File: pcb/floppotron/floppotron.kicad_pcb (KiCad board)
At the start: 2 copper layers, 100 x 92 mm, 69 parts, among them J1 DIN-5_180degree, J10 Conn_01x02, J11 Conn_01x02, J2 Conn_01x02, J3 Conn_01x02, J4 Conn_01x02, J5 Conn_01x02, J6 Conn_01x02, J7 Conn_01x02, J8 AudioJack2, J9 USB_B, Q1 BC817, Q10 2N5457, Q11 BC817, Q12 BC817, Q14 BC817, Q15 BC817, Q16 BC817, Q17 BC817, Q18 BC817, Q19 BC817, Q2 BC817, Q20 BC817, Q3 BC817, Q4 BC817, Q5 BC817, Q6 BC817, Q7 BC817, Q8 BC817, Q9 BC817, U1 H11L1, U2 Pico

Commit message: redesign pcb for pico W
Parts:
- removed C1, C2: C, Capacitor_SMD:C_1206_3216Metric_Pad1.33x1.80mm_HandSolder
- removed J10, J11: Conn_01x02, Connector_JST:JST_XH_B2B-XH-A_1x02_P2.50mm_Vertical
- removed J8: AudioJack2, Connector_Audio:Jack_6.35mm_Neutrik_NRJ4HF_Horizontal
- removed JP1, JP2: Jumper, Connector_PinHeader_2.54mm:PinHeader_1x02_P2.54mm_Vertical
- removed Q10: 2N5457, Package_TO_SOT_THT:TO-92
- removed R21, R22, R23, R24: R, Resistor_SMD:R_1206_3216Metric_Pad1.30x1.75mm_HandSolder
- added H1: MountingHole_Pad, MountingHole:MountingHole_3.2mm_M3_DIN965_Pad, F.Cu at (54.0, 104.0)
- added H2: MountingHole_Pad, MountingHole:MountingHole_3.2mm_M3_DIN965_Pad, F.Cu at (146.0, 104.0)
- added H3: MountingHole_Pad, MountingHole:MountingHole_3.2mm_M3_DIN965_Pad, F.Cu at (54.0, 188.0)
- added H4: MountingHole_Pad, MountingHole:MountingHole_3.2mm_M3_DIN965_Pad, F.Cu at (146.0, 188.0)
- R1, R2: footprint Resistor_THT:R_Axial_DIN0204_L3.6mm_D1.6mm_P5.08mm_Horizontal -> Resistor_SMD:R_1206_3216Metric_Pad1.30x1.75mm_HandSolder
- U2: footprint pico:RPi_Pico_SMD_TH -> kicad-parts:RPi_Pico_debug_hole_USB_SMD_TH
- moved D1 226.3 mm to (124.7, 128.7), turned to 90 degrees
- moved R1 222.1 mm to (122.4, 125.5), turned to -90 degrees
- moved U1 212.1 mm to (118.4, 127.3), turned to 180 degrees
- moved R2 193.2 mm to (108.0, 124.9), turned to 90 degrees
- moved JP3 191.9 mm to (103.6, 124.5), turned to 180 degrees
- moved J9 178.6 mm to (131.7, 112.1)
- moved J1 178.5 mm to (113.0, 109.7)
- moved FLOPPY1 176.4 mm to (73.9, 179.2)
- moved FLOPPY2 176.4 mm to (84.1, 179.2)
- moved FLOPPY3 176.4 mm to (94.2, 179.2)
- moved FLOPPY4 176.4 mm to (104.4, 179.2)
- moved FLOPPY5 176.4 mm to (114.6, 179.2)
- moved J2 176.4 mm to (104.4, 188.1)
- moved J3 176.4 mm to (73.9, 188.1)
- moved J4 176.4 mm to (94.2, 188.1)
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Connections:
- net Net-(J9-Pad2) renamed D-
- net Net-(J9-Pad3) renamed D+
- net Net-(U1-Pad4) renamed MIDI IN
- net Net-(U1-Pad6) renamed +3V3
- J1 pad 1: Net-(J1-Pad1) -> /VCC_device
- J1 pad 2: Net-(J1-Pad2) -> GND
- J9 pad 1: Net-(J9-Pad1) -> unconnected-(J9-VBUS-Pad1)
- J9 pad 5: unconnected-(J9-Pad5) -> GND
- JP3 pad 1: Net-(J1-Pad1) -> VCC
- JP3 pad 2: VCC -> /VCC_device
- R10 pad 2: Net-(U2-Pad19) -> F0-DIR
- R11 pad 1: Net-(U2-Pad20) -> F0-STEP
- R12 pad 2: Net-(U2-Pad34) -> F5-EN
- R13 pad 2: Net-(U2-Pad32) -> F5-DIR
- R14 pad 1: Net-(U2-Pad31) -> F5-STEP
- R15 pad 2: Net-(U2-Pad29) -> F3-EN
- R16 pad 2: Net-(U2-Pad27) -> F3-DIR
- R17 pad 1: Net-(U2-Pad26) -> F3-STEP
- R18 pad 2: Net-(U2-Pad24) -> F1-EN
- R19 pad 2: Net-(U2-Pad22) -> F1-DIR
- R20 pad 1: Net-(U2-Pad21) -> F1-STEP
- R3 pad 2: Net-(U2-Pad7) -> F4-EN
- R4 pad 2: Net-(U2-Pad9) -> F4-DIR
- R5 pad 1: Net-(U2-Pad10) -> F4-STEP
- R6 pad 1: Net-(U2-Pad15) -> F2-STEP
- R7 pad 2: Net-(U2-Pad14) -> F2-DIR
- R8 pad 2: Net-(U2-Pad12) -> F2-EN
- R9 pad 2: Net-(U2-Pad17) -> F0-EN
- U2 pad 10: Net-(U2-Pad10) -> F5-EN
- U2 pad 11: unconnected-(U2-Pad11) -> F4-STEP
- U2 pad 12: Net-(U2-Pad12) -> F4-DIR
- U2 pad 13: unconnected-(U2-Pad13) -> GND
- U2 pad 14: Net-(U2-Pad14) -> F3-STEP
- U2 pad 15: Net-(U2-Pad15) -> F3-DIR
- U2 pad 16: unconnected-(U2-Pad16) -> F2-STEP
- U2 pad 17: Net-(U2-Pad17) -> F2-DIR
- U2 pad 18: unconnected-(U2-Pad18) -> GND
- U2 pad 19: Net-(U2-Pad19) -> F1-STEP
- U2 pad 20: Net-(U2-Pad20) -> F1-DIR
- U2 pad 21: Net-(U2-Pad21) -> F0-EN
- U2 pad 22: Net-(U2-Pad22) -> F0-DIR
- U2 pad 23: unconnected-(U2-Pad23) -> GND
- U2 pad 24: Net-(U2-Pad24) -> F0-STEP
- U2 pad 25: unconnected-(U2-Pad25) -> F1-EN
- U2 pad 26: Net-(U2-Pad26) -> F2-EN
- U2 pad 27: Net-(U2-Pad27) -> F3-EN
- U2 pad 28: unconnected-(U2-Pad28) -> GND
- U2 pad 29: Net-(U2-Pad29) -> F4-EN
- U2 pad 31: Net-(U2-Pad31) -> unconnected-(U2-GPIO26_ADC0-Pad31)
- U2 pad 32: Net-(U2-Pad32) -> unconnected-(U2-GPIO27_ADC1-Pad32)
- U2 pad 33: unconnected-(U2-Pad33) -> GND
- U2 pad 34: Net-(U2-Pad34) -> unconnected-(U2-GPIO28_ADC2-Pad34)
- U2 pad 7: Net-(U2-Pad7) -> F5-STEP
- U2 pad 8: unconnected-(U2-Pad8) -> GND
- U2 pad 9: Net-(U2-Pad9) -> F5-DIR
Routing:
- net GND: track 282.3 -> 0.00 mm
- net VCC: track 246.3 -> 145.4 mm, vias 1 -> 0
- net F5-EN: track 0.00 -> 69.0 mm
- net F5-DIR: track 0.00 -> 66.3 mm, vias 0 -> 1
- net F5-STEP: track 0.00 -> 62.9 mm, vias 0 -> 1
- net Net-(U2-Pad17): track 60.4 -> 0.00 mm
- net F4-DIR: track 0.00 -> 56.5 mm
- net F4-STEP: track 0.00 -> 55.6 mm, vias 0 -> 1
- net F3-DIR: track 0.00 -> 52.1 mm
- net Net-(U2-Pad19): track 48.5 -> 0.00 mm
- net F3-STEP: track 0.00 -> 47.1 mm, vias 0 -> 1
- net Net-(U2-Pad14): track 46.3 -> 0.00 mm
- net F2-DIR: track 0.00 -> 45.6 mm
- net F4-EN: track 0.00 -> 44.9 mm
- net Net-(U2-Pad9): track 44.7 -> 0.00 mm
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- added copper zone on B.Cu, net GND
- added copper zone on F.Cu, net GND
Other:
- outline, holes or cut-outs redrawn
- board text added: "Floppotron Jr. v0.4 designed by AberDerBart"
- board text removed: "D+"
- board text removed: "D-"
- board text removed: "Floppotron Jr. v0.3 designed by AberDerBart"

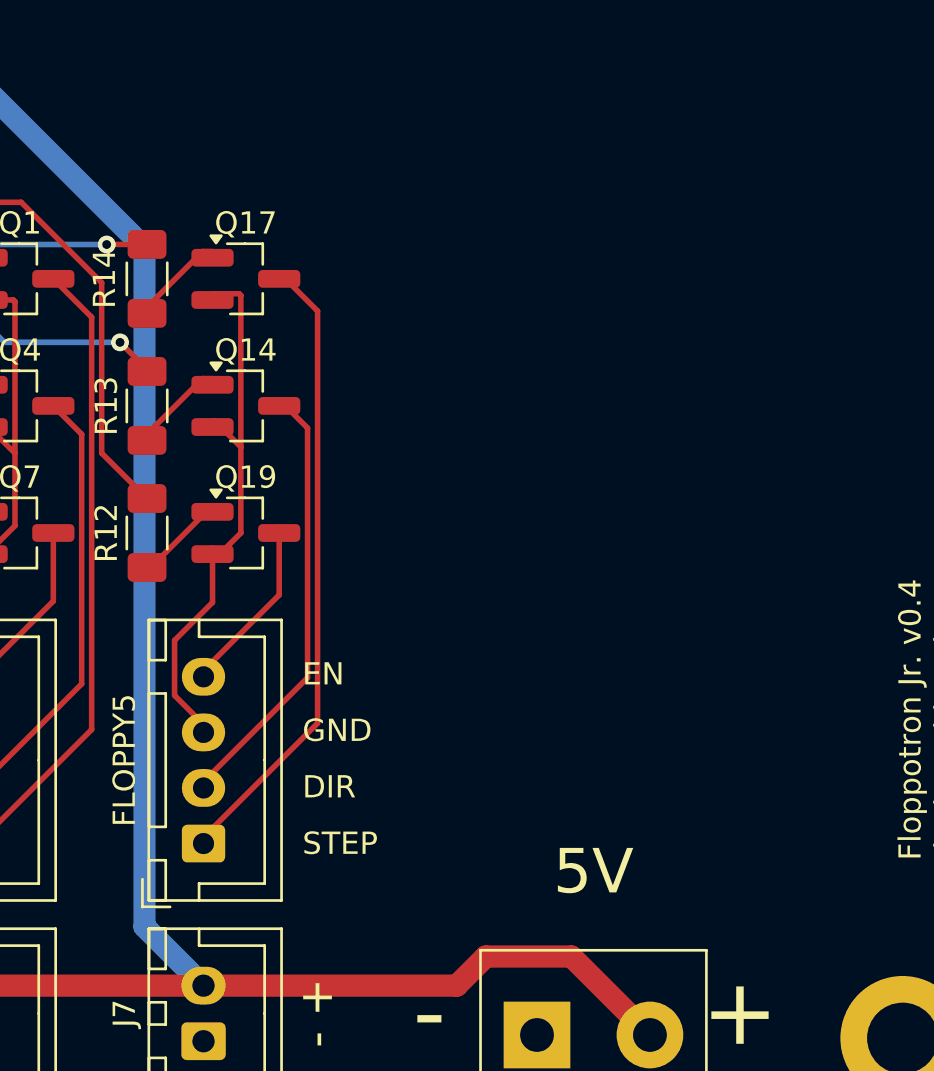
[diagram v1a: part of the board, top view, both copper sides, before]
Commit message: pcb: add kosmo power connector
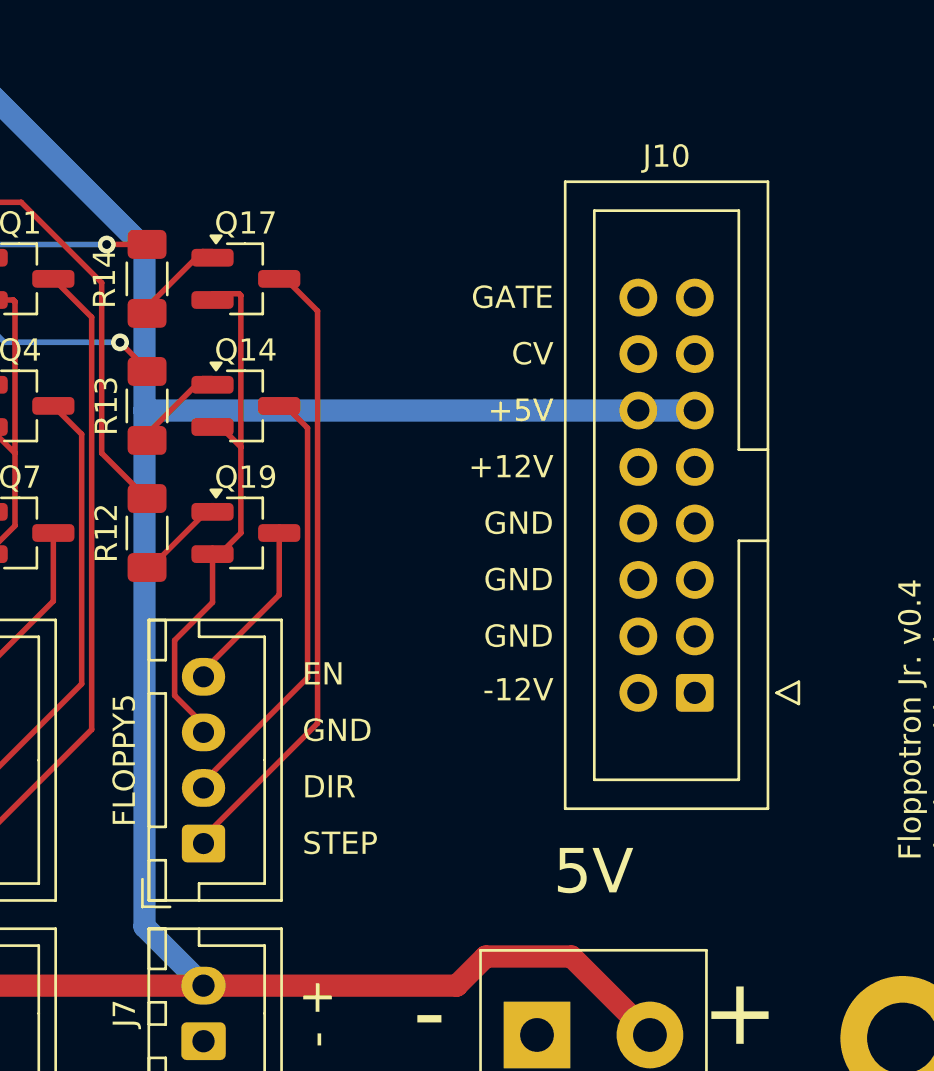
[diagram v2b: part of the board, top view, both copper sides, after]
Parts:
- added J10: Power, kosmo:Power 16 Pin, F.Cu at (135.4, 163.6)
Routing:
- net VCC: track 145.4 -> 170.2 mm
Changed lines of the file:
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@@
   (net 83 "unconnected-(U2-GPIO27_ADC1-Pad32)")
   (net 84 "unconnected-(U2-GPIO26_ADC0-Pad31)")
+  (net 85 "unconnected-(J10--12V-Pad1)")
+  (net 86 "unconnected-(J10-+12V-Pad3)")
+  (net 87 "unconnected-(J10-CV-Pad5)")
+  (net 88 "unconnected-(J10-GATE-Pad6)")
   (footprint "Connector_USB:USB_B_OST_USB-B1HSxx_Horizontal" locked (layer "F.Cu")
     (at 131.7 112.12 90)
@@
       (net 6 "GND") (pinfunction "1") (pintype "input"))
   )
+  (footprint "kosmo:Power 16 Pin" (layer "F.Cu")
+    (at 135.382 163.576)
+    (property "Sheetfile" "floppotron.kicad_sch")
+    (property "Sheetname" "")
+    (attr through_hole)
+    (fp_text reference "J10" (at 0 -15.24 unlocked) (layer "F.SilkS")
+        (effects (font (size 1 1) (thickness 0.15)))
+    )
+    (fp_text value "Power" (at 0 15.24 unlocked) (layer "F.Fab")
+        (effects (font (size 1 1) (thickness 0.15)))
+    )
+    (fp_text user "GND" (at -5.08 3.81 unlocked) (layer "F.SilkS")
+        (effects (font (size 1 1) (thickness 0.15)) (justify right))
+    )
+    (fp_text user "GND" (at -5.08 6.35 unlocked) (layer "F.SilkS")
+        (effects (font (size 1 1) (thickness 0.15)) (justify right))
+    )
+    (fp_text user "-12V" (at -5.08 8.763 unlocked) (layer "F.SilkS")
+        (effects (font (size 1 1) (thickness 0.15)) (justify right))
+    )
+    (fp_text user "CV" (at -5.08 -6.35 unlocked) (layer "F.SilkS")
+        (effects (font (size 1 1) (thickness 0.15)) (justify right))
+    )
+    (fp_text user "GND" (at -5.08 1.27 unlocked) (layer "F.SilkS")
+        (effects (font (size 1 1) (thickness 0.15)) (justify right))
+    )
+    (fp_text user "GATE" (at -5.08 -8.89 unlocked) (layer "F.SilkS")
+        (effects (font (size 1 1) (thickness 0.15)) (justify right))
+    )
+    (fp_text user "+12V" (at -5.08 -1.27 unlocked) (layer "F.SilkS")
+        (effects (font (size 1 1) (thickness 0.15)) (justify right))
+    )
+    (fp_text user "+5V" (at -5.08 -3.81 unlocked) (layer "F.SilkS")
+        (effects (font (size 1 1) (thickness 0.15)) (justify right))
+    )
+    (fp_text user "${REFERENCE}" (at 6.35 0 -90) (layer "F.Fab")
+        (effects (font (size 1 1) (thickness 0.15)))
+    )
+    (fp_line (start -4.56 -14.1) (end 4.56 -14.1)
+      (stroke (width 0.12) (type solid)) (layer "F.SilkS"))
+    (fp_line (start -4.56 14.1) (end -4.56 -14.1)
+      (stroke (width 0.12) (type solid)) (layer "F.SilkS"))
+    (fp_line (start -3.25 -12.8) (end 3.25 -12.8)
+      (stroke (width 0.12) (type solid)) (layer "F.SilkS"))
+    (fp_line (start -3.25 12.8) (end -3.25 -12.8)
+      (stroke (width 0.12) (type solid)) (layer "F.SilkS"))
+    (fp_line (start 3.25 -12.8) (end 3.25 -2.05)
+      (stroke (width 0.12) (type solid)) (layer "F.SilkS"))
+    (fp_line (start 3.25 -2.05) (end 3.25 -2.05)
+      (stroke (width 0.12) (type solid)) (layer "F.SilkS"))
+    (fp_line (start 3.25 -2.05) (end 4.56 -2.05)
+      (stroke (width 0.12) (type solid)) (layer "F.SilkS"))
+    (fp_line (start 3.25 2.05) (end 3.25 12.8)
+      (stroke (width 0.12) (type solid)) (layer "F.SilkS"))
+    (fp_line (start 3.25 12.8) (end -3.25 12.8)
+      (stroke (width 0.12) (type solid)) (layer "F.SilkS"))
+    (fp_line (start 4.56 -14.1) (end 4.56 14.1)
+      (stroke (width 0.12) (type solid)) (layer "F.SilkS"))
+    (fp_line (start 4.56 2.05) (end 3.25 2.05)
+      (stroke (width 0.12) (type solid)) (layer "F.SilkS"))
+    (fp_line (start 4.56 14.1) (end -4.56 14.1)
+      (stroke (width 0.12) (type solid)) (layer "F.SilkS"))
+    (fp_line (start 4.95 8.89) (end 5.95 9.39)
+      (stroke (width 0.12) (type solid)) (layer "F.SilkS"))
+    (fp_line (start 5.95 8.39) (end 4.95 8.89)
+      (stroke (width 0.12) (type solid)) (layer "F.SilkS"))
+    (fp_line (start 5.95 9.39) (end 5.95 8.39)
+      (stroke (width 0.12) (type solid)) (layer "F.SilkS"))
+    (fp_line (start -4.95 -14.49) (end -4.95 14.49)
+      (stroke (width 0.05) (type solid)) (layer "F.CrtYd"))
+    (fp_line (start -4.95 14.49) (end 4.95 14.49)
+      (stroke (width 0.05) (type solid)) (layer "F.CrtYd"))
+    (fp_line (start 4.95 -14.49) (end -4.95 -14.49)
+      (stroke (width 0.05) (type solid)) (layer "F.CrtYd"))
+    (fp_line (start 4.95 14.49) (end 4.95 -14.49)
+      (stroke (width 0.05) (type solid)) (layer "F.CrtYd"))
+    (fp_line (start -4.45 -13.99) (end 4.45 -13.99)
+      (stroke (width 0.1) (type solid)) (layer "F.Fab"))
+    (fp_line (start -4.45 13.99) (end -4.45 -13.99)
+      (stroke (width 0.1) (type solid)) (layer "F.Fab"))
+    (fp_line (start -3.25 -12.8) (end 3.25 -12.8)
+      (stroke (width 0.1) (type solid)) (layer "F.Fab"))
+    (fp_line (start -3.25 12.8) (end -3.25 -12.8)
+      (stroke (width 0.1) (type solid)) (layer "F.Fab"))
+    (fp_line (start 3.25 -12.8) (end 3.25 -2.05)
+      (stroke (width 0.1) (type solid)) (layer "F.Fab"))
+    (fp_line (start 3.25 -2.05) (end 3.25 -2.05)
+      (stroke (width 0.1) (type solid)) (layer "F.Fab"))
+    (fp_line (start 3.25 -2.05) (end 4.45 -2.05)
+      (stroke (width 0.1) (type solid)) (layer "F.Fab"))
+    (fp_line (start 3.25 2.05) (end 3.25 12.8)
+      (stroke (width 0.1) (type solid)) (layer "F.Fab"))
+    (fp_line (start 3.25 12.8) (end -3.25 12.8)
+      (stroke (width 0.1) (type solid)) (layer "F.Fab"))
+    (fp_line (start 3.45 13.99) (end -4.45 13.99)
+      (stroke (width 0.1) (type solid)) (layer "F.Fab"))
+    (fp_line (start 4.45 -13.99) (end 4.45 12.99)
+      (stroke (width 0.1) (type solid)) (layer "F.Fab"))
+    (fp_line (start 4.45 2.05) (end 3.25 2.05)
+      (stroke (width 0.1) (type solid)) (layer "F.Fab"))
+    (fp_line (start 4.45 12.99) (end 3.45 13.99)
+      (stroke (width 0.1) (type solid)) (layer "F.Fab"))
+    (pad "1" thru_hole circle (at -1.27 8.89 180) (size 1.7 1.7) (drill 1) (layers "*.Cu" "*.Mask")
+      (net 85 "unconnected-(J10--12V-Pad1)") (pinfunction "-12V") (pintype "power_out"))
+    (pad "1" thru_hole roundrect (at 1.27 8.89 180) (size 1.7 1.7) (drill 1) (layers "*.Cu" "*.Mask") (roundrect_rratio 0.147059)
+      (net 85 "unconnected-(J10--12V-Pad1)") (pinfunction "-12V") (pintype "power_out"))
+    (pad "2" thru_hole circle (at -1.27 1.27 180) (size 1.7 1.7) (drill 1) (layers "*.Cu" "*.Mask")
+      (net 6 "GND") (pinfunction "GND") (pintype "power_out"))
+    (pad "2" thru_hole circle (at -1.27 3.81 180) (size 1.7 1.7) (drill 1) (layers "*.Cu" "*.Mask")
+      (net 6 "GND") (pinfunction "GND") (pintype "power_out"))
+    (pad "2" thru_hole circle (at -1.27 6.35 180) (size 1.7 1.7) (drill 1) (layers "*.Cu" "*.Mask")
+      (net 6 "GND") (pinfunction "GND") (pintype "power_out"))
+    (pad "2" thru_hole circle (at 1.27 1.27 180) (size 1.7 1.7) (drill 1) (layers "*.Cu" "*.Mask")
+      (net 6 "GND") (pinfunction "GND") (pintype "power_out"))
+    (pad "2" thru_hole circle (at 1.27 3.81 180) (size 1.7 1.7) (drill 1) (layers "*.Cu" "*.Mask")
+      (net 6 "GND") (pinfunction "GND") (pintype "power_out"))
+    (pad "2" thru_hole circle (at 1.27 6.35 180) (size 1.7 1.7) (drill 1) (layers "*.Cu" "*.Mask")
+      (net 6 "GND") (pinfunction "GND") (pintype "power_out"))
+    (pad "3" thru_hole circle (at -1.27 -1.27 180) (size 1.7 1.7) (drill 1) (layers "*.Cu" "*.Mask")
+      (net 86 "unconnected-(J10-+12V-Pad3)") (pinfunction "+12V") (pintype "power_out"))
+    (pad "3" thru_hole circle (at 1.27 -1.27 180) (size 1.7 1.7) (drill 1) (layers "*.Cu" "*.Mask")
+      (net 86 "unconnected-(J10-+12V-Pad3)") (pinfunction "+12V") (pintype "power_out"))
+    (pad "4" thru_hole circle (at -1.27 -3.81 180) (size 1.7 1.7) (drill 1) (layers "*.Cu" "*.Mask")
+      (net 5 "VCC") (pinfunction "+5V") (pintype "power_out"))
+    (pad "4" thru_hole circle (at 1.27 -3.81 180) (size 1.7 1.7) (drill 1) (layers "*.Cu" "*.Mask")
+      (net 5 "VCC") (pinfunction "+5V") (pintype "power_out"))
+    (pad "5" thru_hole circle (at -1.27 -6.35 180) (size 1.7 1.7) (drill 1) (layers "*.Cu" "*.Mask")
+      (net 87 "unconnected-(J10-CV-Pad5)") (pinfunction "CV") (pintype "bidirectional"))
+    (pad "5" thru_hole circle (at 1.27 -6.35 180) (size 1.7 1.7) (drill 1) (layers "*.Cu" "*.Mask")
+      (net 87 "unconnected-(J10-CV-Pad5)") (pinfunction "CV") (pintype "bidirectional"))
+    (pad "6" thru_hole circle (at -1.27 -8.89 180) (size 1.7 1.7) (drill 1) (layers "*.Cu" "*.Mask")
+      (net 88 "unconnected-(J10-GATE-Pad6)") (pinfunction "GATE") (pintype "bidirectional"))
+    (pad "6" thru_hole circle (at 1.27 -8.89 180) (size 1.7 1.7) (drill 1) (layers "*.Cu" "*.Mask")
+      (net 88 "unconnected-(J10-GATE-Pad6)") (pinfunction "GATE") (pintype "bidirectional"))
+  )
   (footprint "eurocad:MIDI_DIN5" locked (layer "F.Cu")
     (at 113 109.7 180)
@@
   (segment (start 125.944 185.634) (end 127.254 184.324) (width 1) (layer "F.Cu") (net 5))
   (segment (start 114.554 185.634) (end 125.944 185.634) (width 1) (layer "F.Cu") (net 5))
+  (segment (start 136.652 159.766) (end 111.9 159.766) (width 1) (layer "B.Cu") (net 5))
+  (segment (start 111.9 152.444365) (end 111.9 159.766) (width 1) (layer "B.Cu") (net 5))
+  (segment (start 111.9 159.766) (end 111.9 182.98) (width 1) (layer "B.Cu") (net 5))
   (segment (start 103.6 124.5) (end 103.6 126.016) (width 1) (layer "B.Cu") (net 5))
   (segment (start 97.536 132.08) (end 97.536 141.186) (width 1) (layer "B.Cu") (net 5))
   (segment (start 97.536 141.186) (end 99.86 143.51) (width 1) (layer "B.Cu") (net 5))
-  (segment (start 111.9 152.444365) (end 111.9 182.98) (width 1) (layer "B.Cu") (net 5))
   (segment (start 102.965635 143.51) (end 111.9 152.444365) (width 1) (layer "B.Cu") (net 5))
   (segment (start 99.86 143.51) (end 102.965635 143.51) (width 1) (layer "B.Cu") (net 5))
